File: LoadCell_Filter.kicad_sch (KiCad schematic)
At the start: 14 parts

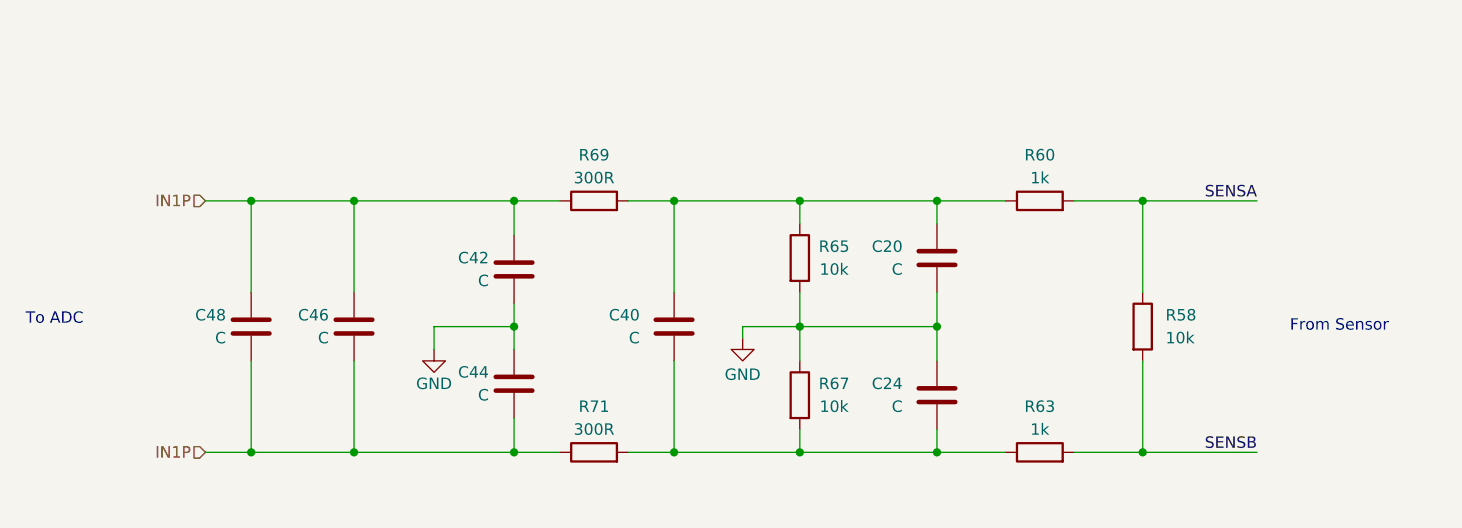
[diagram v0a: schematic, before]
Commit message: Se culmina en que se utilizarà un filtro a  1.5khz para el sensor con divisor de 10k para la entrada ananaloga para el adc externo
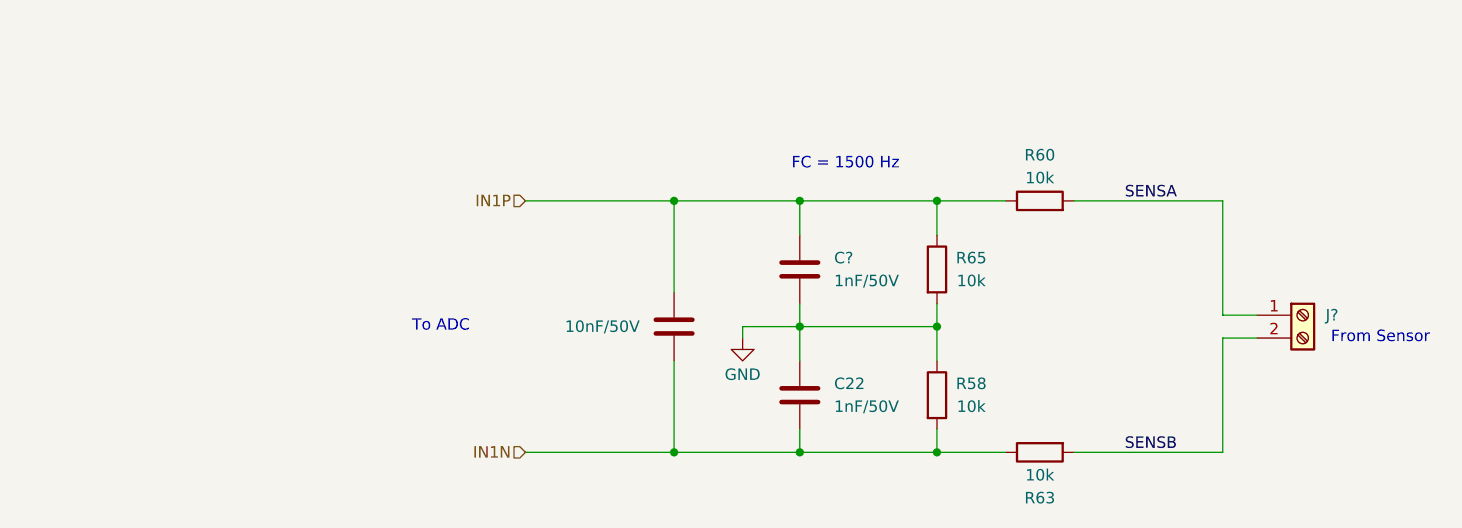
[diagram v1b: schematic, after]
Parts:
- removed C24, C42, C44, C46, C48: C, symbol Device:C
- removed R67: 10k, symbol Device:R
- removed R69, R71: 300R, symbol Device:R
- added C22: 1nF/50V, symbol Device:C
- added J?: Screw_Terminal_01x02, symbol Connector:Screw_Terminal_01x02
- C40: value C -> 10nF/50V
- C?: renamed from C20; value C -> 1nF/50V
- R60, R63: value 1k -> 10k
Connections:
- net GND: now also R58.1, C22.1
- net IN1P: now also C40.1, C?.1, R60.1, R65.1
- net SENSA: now also J?.1 (Pin_1); no longer R58.1
- net SENSB: now also J?.2 (Pin_2); no longer R58.2
- net IN1N: now reaches C40.2, R63.1
- net IN1N: now also R58.2, C22.2
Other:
- note added: "FC = 1500 Hz"
- moved on the sheet: C?, R65

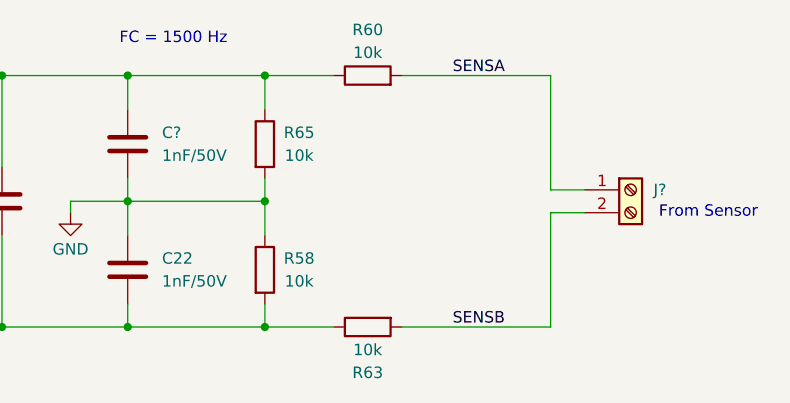
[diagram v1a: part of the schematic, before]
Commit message: Se termina el circuito de entrada análoga, se escoge la bornera. Se termina las salidas de rele, se asumen que se trabajara maximo a 220V y solo para activar contactores. El circuito para el sensor namur se esta realizando
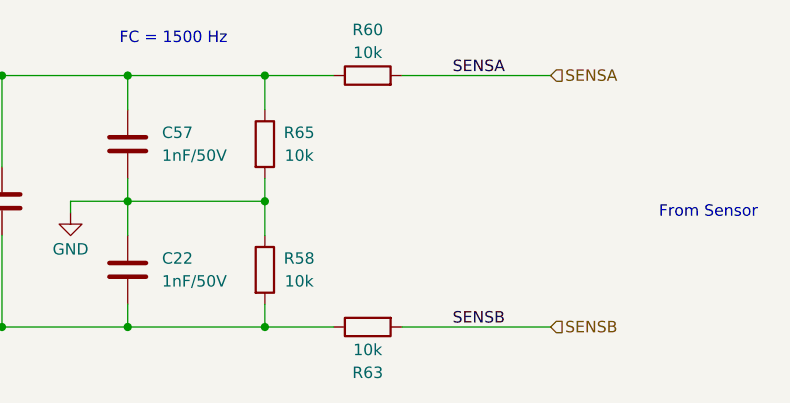
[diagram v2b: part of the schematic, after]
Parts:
- removed J?: Screw_Terminal_01x02, symbol Connector:Screw_Terminal_01x02
- gave numbers to parts that had none: 1

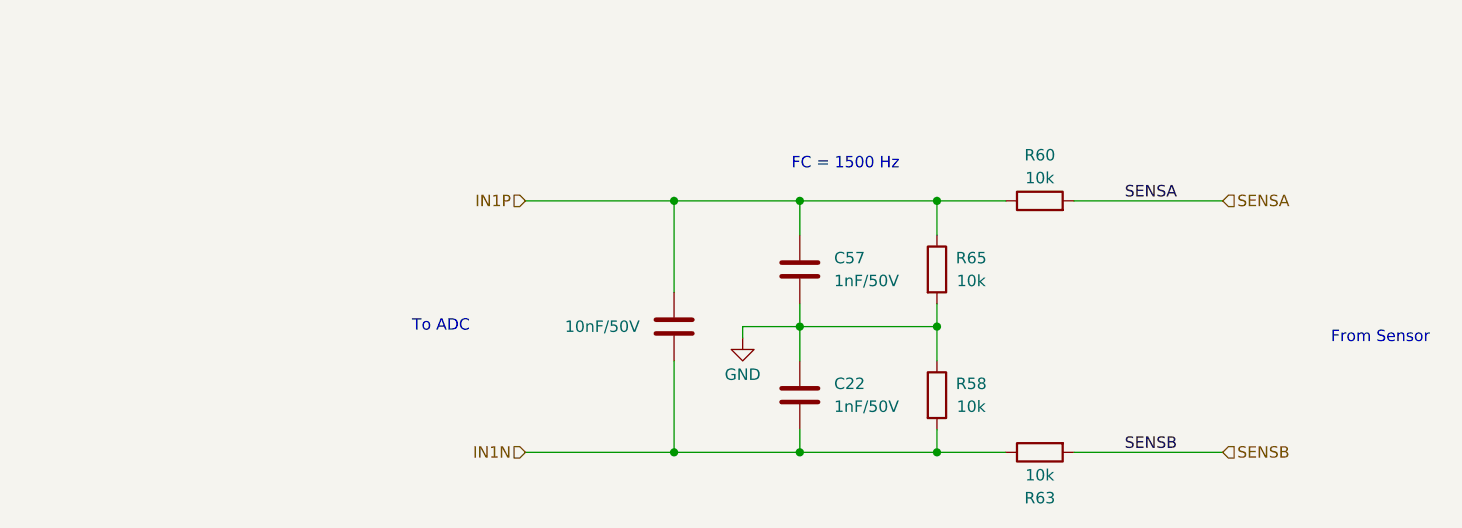
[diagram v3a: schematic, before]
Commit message: avance de pcb, se considera borneras externas para conexión de alimentación
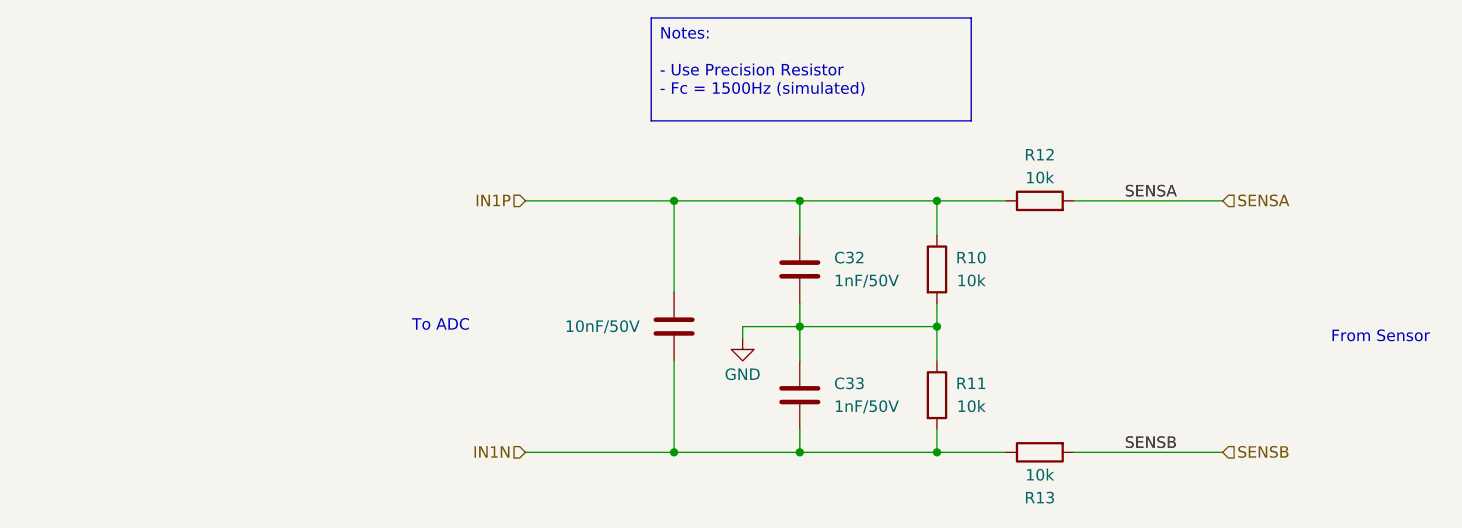
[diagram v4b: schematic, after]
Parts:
- C31: renamed from C40; footprint (none) -> Capacitor_SMD:C_0603_1608Metric
- C32: renamed from C57; footprint (none) -> Capacitor_SMD:C_0603_1608Metric
- C33: renamed from C22; footprint (none) -> Capacitor_SMD:C_0603_1608Metric
- R10: renamed from R65; footprint (none) -> Resistor_SMD:R_0603_1608Metric
- R11: renamed from R58; footprint (none) -> Resistor_SMD:R_0603_1608Metric
- R12: renamed from R60; footprint (none) -> Resistor_SMD:R_0603_1608Metric
- R13: renamed from R63; footprint (none) -> Resistor_SMD:R_0603_1608Metric
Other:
- note removed: "FC = 1500 Hz"
